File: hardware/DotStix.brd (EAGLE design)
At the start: 20.3 x 50 mm, 32 parts, among them IC1 CAT24M010TS, IC2 SI1145, U1 ATMEGA328P-MU-QFN32, U2 TMP102, U4 9DoF IMU

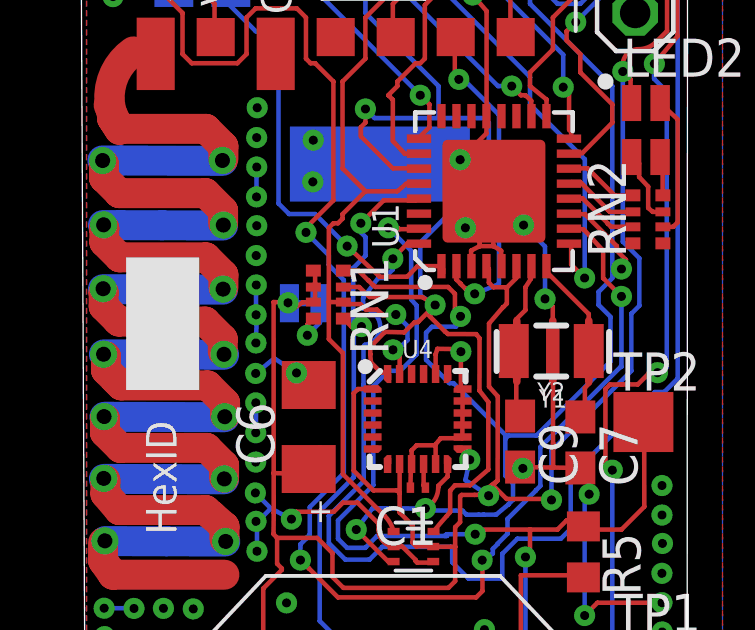
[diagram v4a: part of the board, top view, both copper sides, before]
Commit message: Remove unnecessary solder jumper
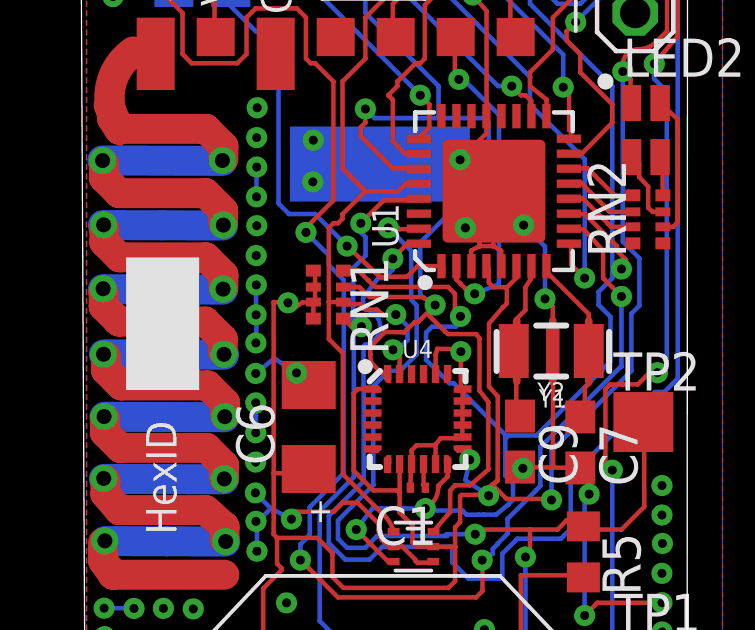
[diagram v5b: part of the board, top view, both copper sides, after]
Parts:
- removed SJ1: SOLDERJUMPERTRACE, SparkFun:SJ_2S-TRACE
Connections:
- removed net N$5: RN1.8, SJ1.1
- net +3V3: now also RN1.8; no longer SJ1.2
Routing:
- net N$5: track 1.88 -> 0.00 mm, vias 1 -> 0
- net +3V3: track 161.1 -> 161.8 mm
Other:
- board text added: "DotStix v0.4.2"
- board text removed: "DotStix v0.4.1"
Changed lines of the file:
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@@
 <rectangle x1="7.4803" y1="9.8679" x2="8.6487" y2="9.8933" layer="22" rot="R180"/>
 <text x="4.983478125" y="43.2206375" size="1.27" layer="22" rot="MR270" align="center">Mihai Galos</text>
-<text x="9.6774" y="11.4046" size="1.016" layer="22" rot="MR0" align="center">DotStix v0.4.1</text>
+<text x="9.6774" y="11.4046" size="1.016" layer="22" rot="MR0" align="center">DotStix v0.4.2</text>
 <circle x="17.2974" y="30.7848" radius="0.193440625" width="0.1524" layer="21"/>
 <circle x="17.27961875" y="30.7848" radius="0.071840625" width="0.1524" layer="21"/>
@@
 <element name="R5" library="resistor" package="R0603" value="470kΩ" x="16.5633375" y="15.10538125" rot="R270"/>
 <element name="C6" library="adafruit" package="C3216" value="100uF 4V" x="7.406640625" y="19.2684375" rot="R90"/>
-<element name="SJ1" library="SparkFun" package="SJ_2S-TRACE" value="SOLDERJUMPERTRACE" x="7.27201875" y="23.395940625" rot="MR0"/>
 <element name="U$3" library="pusbbutton_4x2_5" package="PUSHBUTTON_4X2.5" value="PUSHBUTTON_4X2.5" x="18.39468125" y="3.1115" rot="R270"/>
 <element name="RN1" library="resistor-dil" package="4X0402ARV341" value="4.7kΩ" x="8.0619625" y="23.682959375" rot="R90">
@@
 <contactref element="TP5" pad="TP"/>
 <wire x1="5.67181875" y1="28.915359375" x2="5.6896" y2="29.911040625" width="0" layer="19" extent="1-1"/>
-<wire x1="5.65911875" y1="24.003" x2="5.656578125" y2="24.983440625" width="0" layer="19" extent="1-1"/>
 </signal>
 <signal name="SDA">
@@
 <contactref element="R5" pad="2"/>
 <contactref element="C6" pad="1"/>
-<contactref element="SJ1" pad="2"/>
 <contactref element="RN1" pad="7"/>
 <contactref element="RN1" pad="6"/>
@@
 <via x="6.715759375" y="23.408640625" extent="1-16" drill="0.3"/>
 <wire x1="6.715759375" y1="23.408640625" x2="6.581140625" y2="23.41118125" width="0.1524" layer="16"/>
-<wire x1="6.581140625" y1="23.41118125" x2="6.76401875" y2="23.395940625" width="0.1524" layer="16"/>
 <wire x1="7.62" y1="17.34058125" x2="7.25678125" y2="17.7038" width="0.1524" layer="1"/>
 <wire x1="7.25678125" y1="17.7038" x2="6.238240625" y2="17.731740625" width="0.1524" layer="1"/>
@@
 <wire x1="11.40968125" y1="39.359840625" x2="11.40968125" y2="37.92728125" width="0.1524" layer="1"/>
 <wire x1="11.40968125" y1="37.92728125" x2="7.9248" y2="34.4424" width="0.1524" layer="1"/>
-<wire x1="6.76401875" y1="23.395940625" x2="6.939278125" y2="23.238459375" width="0" layer="19" extent="1-16"/>
+<contactref element="RN1" pad="8"/>
+<wire x1="7.5619625" y1="22.882959375" x2="7.5619625" y2="23.432959375" width="0.1524" layer="1"/>
+<wire x1="6.939278125" y1="23.238459375" x2="6.885940625" y2="23.238459375" width="0.1524" layer="1"/>
+<wire x1="6.885940625" y1="23.238459375" x2="6.715759375" y2="23.408640625" width="0.1524" layer="1"/>
 </signal>
 <signal name="MOSI">
@@
 <wire x1="18.2111" y1="25.94101875" x2="18.212178125" y2="25.939940625" width="0.1524" layer="1"/>
 </signal>
-<signal name="N$5">
-<contactref element="SJ1" pad="1"/>
-<contactref element="RN1" pad="8"/>
-<wire x1="7.5619625" y1="22.882959375" x2="7.36091875" y2="22.681915625" width="0.1524" layer="1"/>
-<wire x1="7.36091875" y1="22.681915625" x2="7.36091875" y2="22.3266" width="0.1524" layer="1"/>
-<via x="7.36091875" y="22.3266" extent="1-16" drill="0.3"/>
-<wire x1="7.36091875" y1="22.3266" x2="7.78001875" y2="22.7457" width="0.1524" layer="16"/>
-<wire x1="7.78001875" y1="22.7457" x2="7.78001875" y2="23.395940625" width="0.1524" layer="16"/>
-</signal>
 <signal name="INT_MULTIPLE">

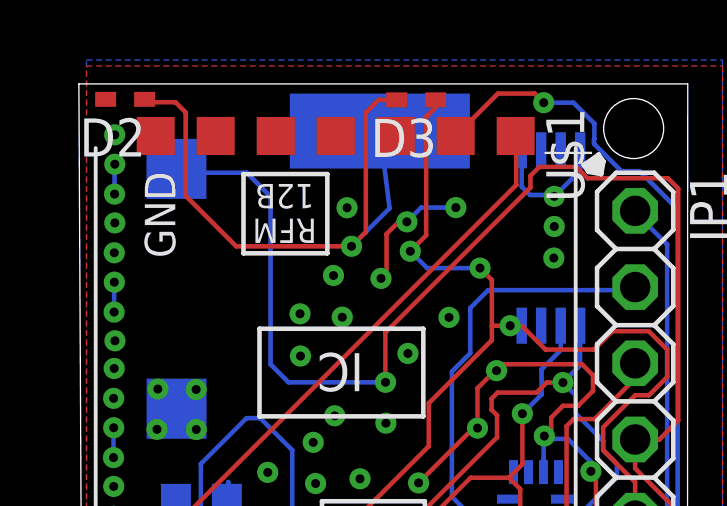
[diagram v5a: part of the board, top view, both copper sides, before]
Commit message: Move 3V3 Zener to low side of Schottky
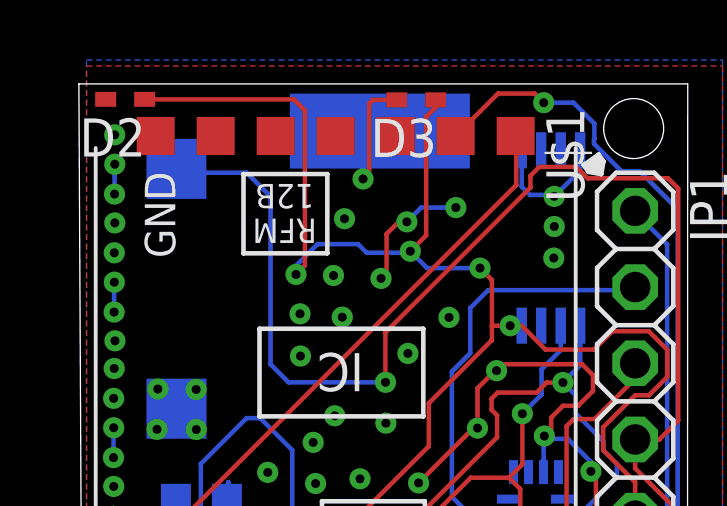
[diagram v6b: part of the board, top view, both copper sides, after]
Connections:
- removed net SOLAR_RAW: D1.+, D2.C, D3.A
- new net N$2: D1.+, D3.A
- net +3V3: now also D2.C
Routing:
- net SOLAR_RAW: track 20.8 -> 0.00 mm, vias 1 -> 0
- net +3V3: track 161.8 -> 177.4 mm, vias 10 -> 11
- net N$2: track 0.00 -> 5.47 mm, vias 0 -> 1
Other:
- board text added: "DotStix v0.4.3"
- board text removed: "DotStix v0.4.2"
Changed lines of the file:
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@@
 <rectangle x1="7.4803" y1="9.8679" x2="8.6487" y2="9.8933" layer="22" rot="R180"/>
 <text x="4.983478125" y="43.2206375" size="1.27" layer="22" rot="MR270" align="center">Mihai Galos</text>
-<text x="9.6774" y="11.4046" size="1.016" layer="22" rot="MR0" align="center">DotStix v0.4.2</text>
+<text x="9.6774" y="11.4046" size="1.016" layer="22" rot="MR0" align="center">DotStix v0.4.3</text>
 <circle x="17.2974" y="30.7848" radius="0.193440625" width="0.1524" layer="21"/>
 <circle x="17.27961875" y="30.7848" radius="0.071840625" width="0.1524" layer="21"/>
@@
 <via x="12.311378125" y="45.88001875" extent="1-16" drill="0.3"/>
 <via x="10.67815625" y="45.405040625" extent="1-16" drill="0.3"/>
-<via x="8.684259375" y="45.874940625" extent="1-16" drill="0.3"/>
+<via x="8.6004375" y="45.50918125" extent="1-16" drill="0.3"/>
 <wire x1="10.67815625" y1="45.405040625" x2="11.153134375" y2="45.88001875" width="0.1524" layer="16"/>
 <wire x1="11.153134375" y1="45.88001875" x2="12.311378125" y2="45.88001875" width="0.1524" layer="16"/>
@@
 <wire x1="6.939278125" y1="23.238459375" x2="6.885940625" y2="23.238459375" width="0.1524" layer="1"/>
 <wire x1="6.885940625" y1="23.238459375" x2="6.715759375" y2="23.408640625" width="0.1524" layer="1"/>
+<contactref element="D2" pad="C"/>
+<wire x1="1.938575" y1="49.486821875" x2="6.9113375" y2="49.486821875" width="0.1524" layer="1"/>
+<wire x1="6.9113375" y1="49.486821875" x2="7.279640625" y2="49.11851875" width="0.1524" layer="1"/>
+<wire x1="7.279640625" y1="49.11851875" x2="7.279640625" y2="43.949621875" width="0.1524" layer="1"/>
+<wire x1="7.279640625" y1="43.949621875" x2="6.982459375" y2="43.652440625" width="0.1524" layer="1"/>
+<via x="6.982459375" y="43.652440625" extent="1-16" drill="0.3"/>
+<wire x1="6.982459375" y1="43.652440625" x2="6.982459375" y2="43.9445375" width="0.1524" layer="16"/>
+<wire x1="6.982459375" y1="43.9445375" x2="7.70128125" y2="44.663359375" width="0.1524" layer="16"/>
+<wire x1="7.70128125" y1="44.663359375" x2="9.050021875" y2="44.663359375" width="0.1524" layer="16"/>
+<wire x1="9.050021875" y1="44.663359375" x2="9.33958125" y2="44.3738" width="0.1524" layer="16"/>
+<wire x1="9.33958125" y1="44.3738" x2="10.741659375" y2="44.3738" width="0.1524" layer="16"/>
+<wire x1="10.741659375" y1="44.3738" x2="10.792459375" y2="44.4246" width="0.1524" layer="16"/>
 </signal>
 <signal name="MOSI">
@@
 <wire x1="10.457178125" y1="21.14041875" x2="10.071096875" y2="21.14041875" width="0.1524" layer="16"/>
 </signal>
-<signal name="SOLAR_RAW">
-<contactref element="D2" pad="C"/>
-<contactref element="D3" pad="A"/>
-<contactref element="D1" pad="+"/>
-<wire x1="9.778996875" y1="48.43208125" x2="10.101578125" y2="45.857159375" width="0.1524" layer="16"/>
-<wire x1="10.101578125" y1="45.857159375" x2="8.83411875" y2="44.5897" width="0.1524" layer="16"/>
-<via x="8.83411875" y="44.5897" extent="1-16" drill="0.3"/>
-<wire x1="8.83411875" y1="44.5897" x2="4.988559375" y2="44.5897" width="0.1524" layer="1"/>
-<wire x1="4.988559375" y1="44.5897" x2="3.304540625" y2="46.27371875" width="0.1524" layer="1"/>
-<wire x1="3.304540625" y1="46.27371875" x2="3.304540625" y2="49.052478125" width="0.1524" layer="1"/>
-<wire x1="3.304540625" y1="49.052478125" x2="2.96671875" y2="49.3903" width="0.1524" layer="1"/>
-<wire x1="2.96671875" y1="49.3903" x2="2.035096875" y2="49.3903" width="0.1524" layer="1"/>
-<wire x1="2.035096875" y1="49.3903" x2="1.938575" y2="49.486821875" width="0.1524" layer="1"/>
-<wire x1="10.341378125" y1="49.47158125" x2="9.73328125" y2="49.47158125" width="0.1524" layer="1"/>
-<wire x1="9.73328125" y1="49.47158125" x2="9.311640625" y2="49.049940625" width="0.1524" layer="1"/>
-<wire x1="9.311640625" y1="49.049940625" x2="9.311640625" y2="45.067221875" width="0.1524" layer="1"/>
-<wire x1="9.311640625" y1="45.067221875" x2="8.83411875" y2="44.5897" width="0.1524" layer="1"/>
-</signal>
 <signal name="LIGHT_SENSE">
 <contactref element="U1" pad="1"/>
@@
 <wire x1="11.23630625" y1="17.3169125" x2="11.23630625" y2="18.035140625" width="0.1524" layer="1"/>
 </signal>
+<signal name="N$2">
+<contactref element="D3" pad="A"/>
+<contactref element="D1" pad="+"/>
+<wire x1="10.341378125" y1="49.47158125" x2="9.552940625" y2="49.47158125" width="0.1524" layer="1"/>
+<wire x1="9.552940625" y1="49.47158125" x2="9.4234" y2="49.342040625" width="0.1524" layer="1"/>
+<wire x1="9.4234" y1="49.342040625" x2="9.4234" y2="46.890940625" width="0.1524" layer="1"/>
+<wire x1="9.4234" y1="46.890940625" x2="9.217659375" y2="46.8350625" width="0.1524" layer="1"/>
+<via x="9.217659375" y="46.8350625" extent="1-16" drill="0.3"/>
+<wire x1="9.217659375" y1="46.8350625" x2="9.2075" y2="47.860584375" width="0.1524" layer="16"/>
+<wire x1="9.2075" y1="47.860584375" x2="9.778996875" y2="48.43208125" width="0.1524" layer="16"/>
+</signal>
 </signals>

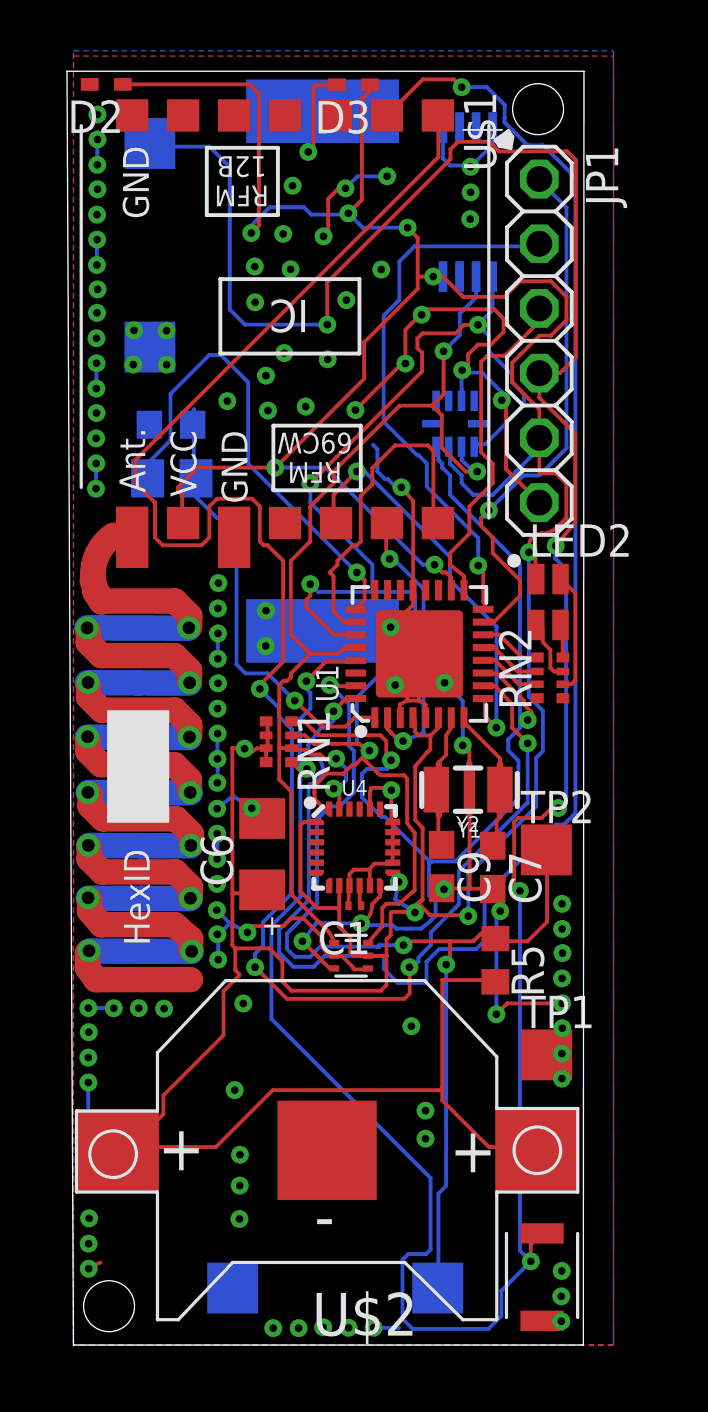
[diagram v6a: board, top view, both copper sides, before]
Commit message: Add infos to minimize power
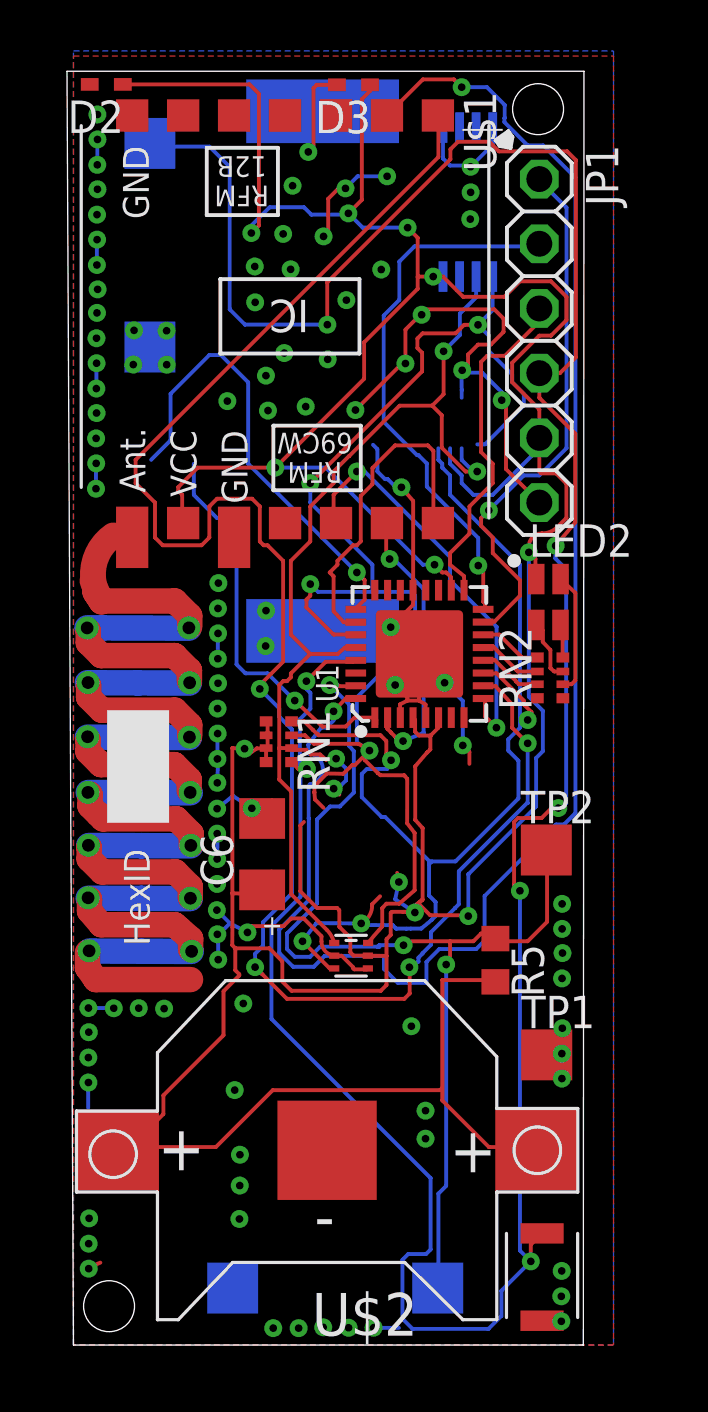
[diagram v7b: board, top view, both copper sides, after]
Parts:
- removed C1: 0.1uF, rcl:C0201
- removed C7, C9: 7pF, rcl:C0603
- removed IC2: SI1145, silabs:QFN-10
- removed R3: (no value), resistor:R0805
- removed R4: 10kΩ, resistor:R0603
- removed U4: 9DoF IMU, SparkFun-Sensors:QFN24-3X3
- removed Y1: (no value), SparkFun-Clocks:RESONATOR-SMD-3.2X1.3
- removed Y2: (no value), SparkFun-Clocks:CRYSTAL-SMD-3.2X1.5MM
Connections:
- removed net N$11: C1.1, U4.10
- removed net XTAL1: C9.1, U1.7, Y1.3, Y2.P$2
- removed net XTAL2: C7.1, U1.8, Y1.1, Y2.P$1
- net +3V3: no longer IC2.3, U4.1, U4.13, U4.8
- net GND: no longer C1.2, C7.2, C9.2, IC2.8, R4.1, U4.11, U4.18, U4.20, U4.9, Y1.2
- net INT_MULTIPLE: no longer IC2.4, U4.12
- net LIGHT_SENSE: no longer R3.1, R4.2
- net LIGHT_SENSE_ENA: no longer R3.2
- net SCL: no longer IC2.2, U4.23
- net SDA: no longer IC2.1, U4.24
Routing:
- net GND: track 96.1 -> 74.0 mm, vias 107 -> 102
- net XTAL1: track 4.37 -> 0.00 mm
- net LIGHT_SENSE: track 19.4 -> 15.5 mm
- net XTAL2: track 3.80 -> 0.00 mm
- net +3V3: track 177.4 -> 175.8 mm
- net N$11: track 0.81 -> 0.00 mm
- net LIGHT_SENSE_ENA: track 18.7 -> 18.0 mm
- net SCL: track 43.4 -> 42.8 mm
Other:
- board text added: "If SI1145, VCC from pin (3.5mA), no sleep"
- board text added: "Investigate powering the TMP112 from a pin, reducing 7uA to 0.2uA consumption. See https://github.com/mihaigalos/fun/tree/master/deep_sleep"
- board text removed: "If you plan on potting the board in transparent epoxy, the battery's max cycle count ist 1000. Use a 330mF Supercap instead of battery: DSK-3R3H334T-HL"

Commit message: Add NMOS to minimize leakage through 100uF cap
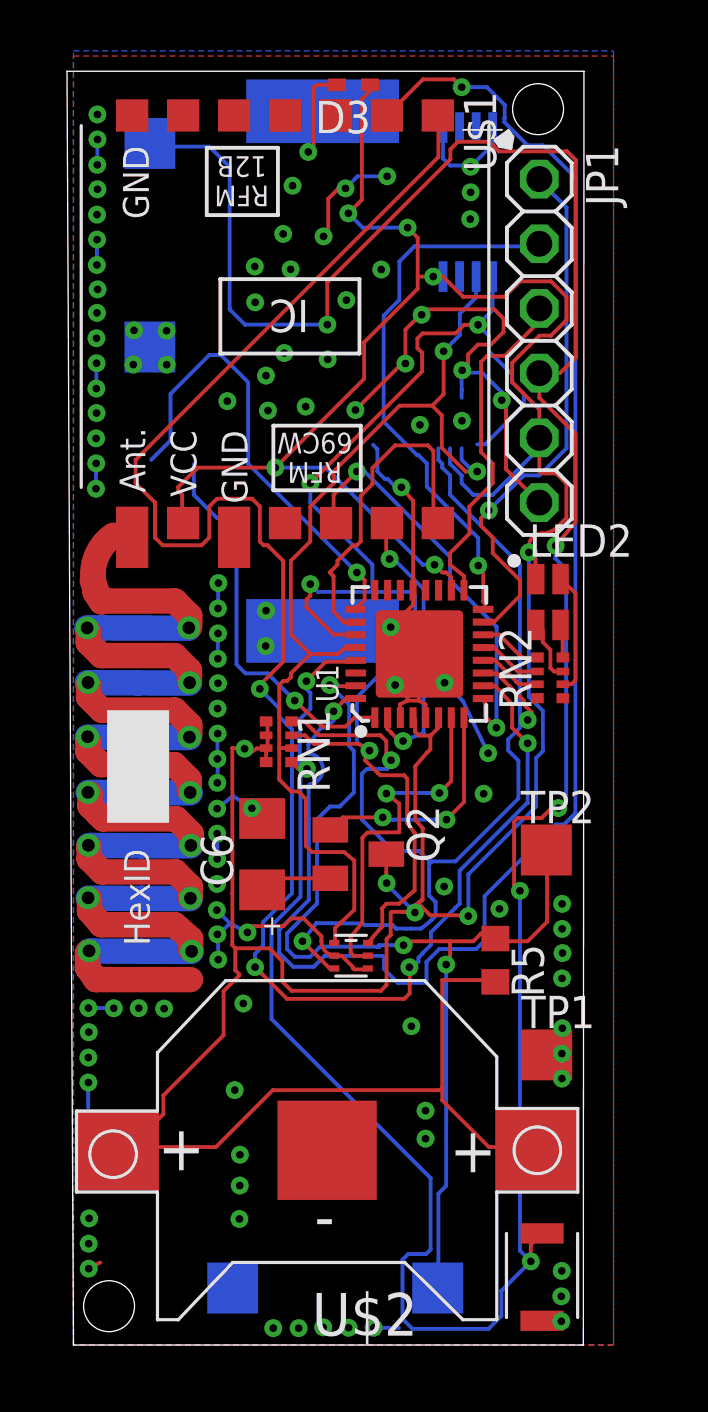
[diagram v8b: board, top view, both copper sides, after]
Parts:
- removed D2: (no value), diode:SOD523
- added Q2: BSH103, adafruit:SOT23
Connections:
- new net N$5: C6.1, Q2.2
- new net TMP112_VCC: U1.7, U2.5
- new net VCC_100UF_CAP: Q2.1, U1.8
- net +3V3: now also Q2.3; no longer C6.1, D2.C, U2.5
- net GND: no longer D2.A
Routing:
- net +3V3: track 175.8 -> 149.7 mm, vias 11 -> 10
- net TMP112_VCC: track 0.00 -> 13.9 mm, vias 0 -> 2
- net VCC_100UF_CAP: track 0.00 -> 9.10 mm, vias 0 -> 2
- net SDA: track 56.5 -> 52.8 mm
- net GND: track 74.0 -> 77.1 mm, vias 102 -> 107
- net N$5: track 0.00 -> 2.86 mm
- net SCL: track 42.8 -> 40.6 mm, vias 4 -> 2
- net INT_MULTIPLE: track 45.4 -> 44.5 mm, vias 4 -> 3
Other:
- board text removed: "Investigate powering the TMP112 from a pin, reducing 7uA to 0.2uA consumption. See https://github.com/mihaigalos/fun/tree/master/deep_sleep"
